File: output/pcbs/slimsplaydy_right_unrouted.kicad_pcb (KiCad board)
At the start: 2 copper layers, 123 x 89.4 mm, 20 parts

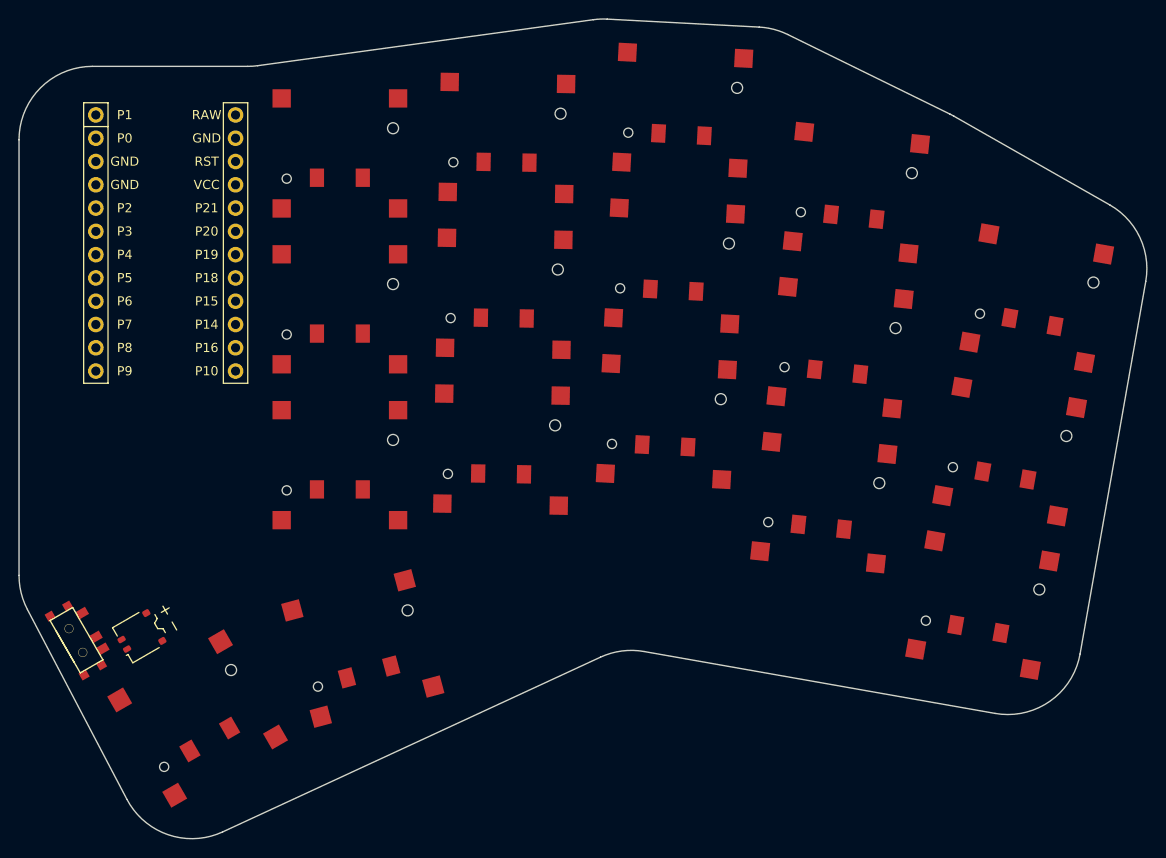
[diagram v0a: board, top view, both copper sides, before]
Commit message: Add battery footprint, change outline.
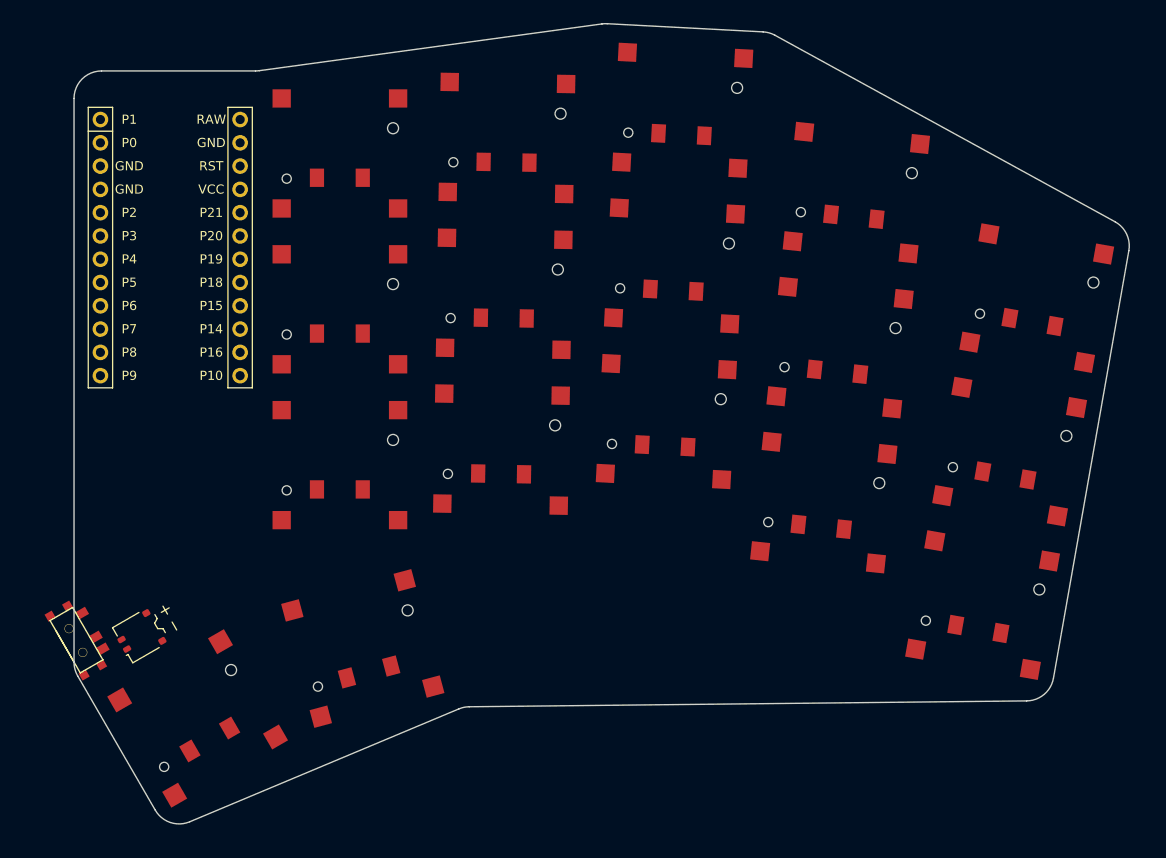
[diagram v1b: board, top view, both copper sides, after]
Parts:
- moved MCU1 0.71 mm to (240.2, 103.4)
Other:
- board size 123 x 89.4 mm -> 115.1 x 87.3 mm
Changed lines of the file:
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@@
   (footprint "ceoloide:mcu_nice_nano"
     (layer "F.Cu")
-    (at 239.71498989999998 102.9119144 0)
+    (at 240.21498989999998 103.4119144 0)
     (property "Reference" "MCU1"
       (at 0 -15 0)
@@
     (fp_line (start 0.45 2.02) (end 0.75 2.52) (layer "F.Fab") (stroke (width 0.1) (type solid)))
   )
-  (gr_line (start 224.62941621776048 144.15640409340858) (end 235.48907572804907 164.87383622286382) (angle 90) (layer Edge.Cuts) (width 0.15))
-(gr_line (start 245.93308625410043 168.4206378744767) (end 287.1447548576141 149.35875036884914) (angle 90) (layer Edge.Cuts) (width 0.15))
-(gr_line (start 291.89237722699136 148.74120448571054) (end 330.1927776020851 155.49459846191698) (angle 90) (layer Edge.Cuts) (width 0.15))
-(gr_line (start 339.4604251055098 149.00532200962266) (end 346.62555657595624 108.36984239288972) (angle 90) (layer Edge.Cuts) (width 0.15))
-(gr_line (start 342.70527937957957 100.02847929984773) (end 325.7106311637271 90.35266764826031) (angle 90) (layer Edge.Cuts) (width 0.15))
-(gr_line (start 325.27590068376344 90.12255661648267) (end 307.56559273611055 81.43431461843029) (angle 90) (layer Edge.Cuts) (width 0.15))
-(gr_line (start 304.46082644944914 80.627566934186) (end 287.8770321181828 79.75844707558387) (angle 90) (layer Edge.Cuts) (width 0.15))
-(gr_line (start 286.3725248782728 79.8215135762144) (end 249.7553757119896 84.83788418286846) (angle 90) (layer Edge.Cuts) (width 0.15))
-(gr_line (start 248.66955648693747 84.9119144) (end 231.71498989999998 84.9119144) (angle 90) (layer Edge.Cuts) (width 0.15))
-(gr_line (start 223.71498989999998 92.9119144) (end 223.71498989999998 140.44228965030038) (angle 90) (layer Edge.Cuts) (width 0.15))
-(gr_arc (start 242.5746494102886 161.15972177975567) (end 235.4890757102886 164.87383617975567) (angle -87.15963248931939) (layer Edge.Cuts) (width 0.15))
-(gr_arc (start 290.5031917014261 156.61966646357) (end 291.8923772014261 148.74120446357) (angle -34.82225270838096) (layer Edge.Cuts) (width 0.15))
-(gr_arc (start 331.58196312765034 147.6161364840575) (end 330.19277762765034 155.49459848405752) (angle -90.00000000000074) (layer Edge.Cuts) (width 0.15))
-(gr_arc (start 338.74709459809674 106.98065686732457) (end 346.62555659809675 108.36984236732457) (angle -70.34521145838565) (layer Edge.Cuts) (width 0.15))
-(gr_arc (start 321.75244638224416 97.30484521573734) (end 325.7106311822442 90.35266761573735) (angle -3.5233551442788595) (layer Edge.Cuts) (width 0.15))
-(gr_arc (start 304.0421384345913 88.61660321768503) (end 307.56559273459135 81.43431461768503) (angle -23.13143158211235) (layer Edge.Cuts) (width 0.15))
-(gr_arc (start 287.45834410332503 87.74748335908288) (end 287.877032103325 79.75844705908288) (angle -10.800686763770258) (layer Edge.Cuts) (width 0.15))
-(gr_arc (start 248.66955648693747 76.9119144) (end 248.66955648693747 84.9119144) (angle -7.80068415589335) (layer Edge.Cuts) (width 0.15))
-(gr_arc (start 231.71498989999998 92.9119144) (end 231.71498989999998 84.9119144) (angle -90) (layer Edge.Cuts) (width 0.15))
-(gr_arc (start 231.71498989999998 140.44228965030038) (end 223.71498989999998 140.44228965030038) (angle -27.662619426405428) (layer Edge.Cuts) (width 0.15))
+  (gr_line (start 230.1175815749614 151.40850733128238) (end 238.5801595902031 166.05106761935943) (angle 90) (layer Edge.Cuts) (width 0.15))
+(gr_line (start 242.33790013594952 167.31643081205561) (end 271.69614917873605 155.00300961504507) (angle 90) (layer Edge.Cuts) (width 0.15))
+(gr_line (start 272.82490909840277 154.76969506548124) (end 333.63407919619016 154.1297000430115) (angle 90) (layer Edge.Cuts) (width 0.15))
+(gr_line (start 336.5569301810632 151.65081072395856) (end 344.78078664705345 105.01100333847262) (angle 90) (layer Edge.Cuts) (width 0.15))
+(gr_line (start 343.26885093801934 101.85961590074882) (end 306.1712679713268 81.51597017246684) (angle 90) (layer Edge.Cuts) (width 0.15))
+(gr_line (start 304.8857883993991 81.1505244358074) (end 287.87730349162115 80.25914752326051) (angle 90) (layer Edge.Cuts) (width 0.15))
+(gr_line (start 287.3147927018884 80.28256782932583) (end 249.91680642992333 85.38438268843433) (angle 90) (layer Edge.Cuts) (width 0.15))
+(gr_line (start 249.51130364514313 85.4119144) (end 232.71498989999998 85.4119144) (angle 90) (layer Edge.Cuts) (width 0.15))
+(gr_line (start 229.71498989999998 88.4119144) (end 229.71498989999998 149.90735117460588) (angle 90) (layer Edge.Cuts) (width 0.15))
+(gr_arc (start 241.17756791524167 164.54991146268293) (end 238.58015951524166 166.05106766268293) (angle -82.72862751199239) (layer Edge.Cuts) (width 0.15))
+(gr_arc (start 272.856481399444 157.76952896441782) (end 272.824909099444 154.76969506441782) (angle -22.151130378445146) (layer Edge.Cuts) (width 0.15))
+(gr_arc (start 333.60250689514885 151.12986614407492) (end 333.63407919514884 154.12970004407492) (angle -79.39700155068272) (layer Edge.Cuts) (width 0.15))
+(gr_arc (start 341.82636336113904 104.49005875858893) (end 344.780786661139 105.01100335858894) (angle -71.26042897747936) (layer Edge.Cuts) (width 0.15))
+(gr_arc (start 304.72878039444646 84.14641303030704) (end 306.17126799444645 81.51597013030704) (angle -25.739569207299766) (layer Edge.Cuts) (width 0.15))
+(gr_arc (start 287.7202954866686 83.25503611776017) (end 287.8773034866686 80.25914751776017) (angle -10.768313705573433) (layer Edge.Cuts) (width 0.15))
+(gr_arc (start 249.51130364514313 82.4119144) (end 249.51130364514313 85.4119144) (angle -7.768311097697847) (layer Edge.Cuts) (width 0.15))
+(gr_arc (start 232.71498989999998 88.4119144) (end 232.71498989999998 85.4119144) (angle -90) (layer Edge.Cuts) (width 0.15))
+(gr_arc (start 232.71498989999998 149.90735117460588) (end 229.71498989999998 149.90735117460588) (angle -30.025500523112385) (layer Edge.Cuts) (width 0.15))
 )

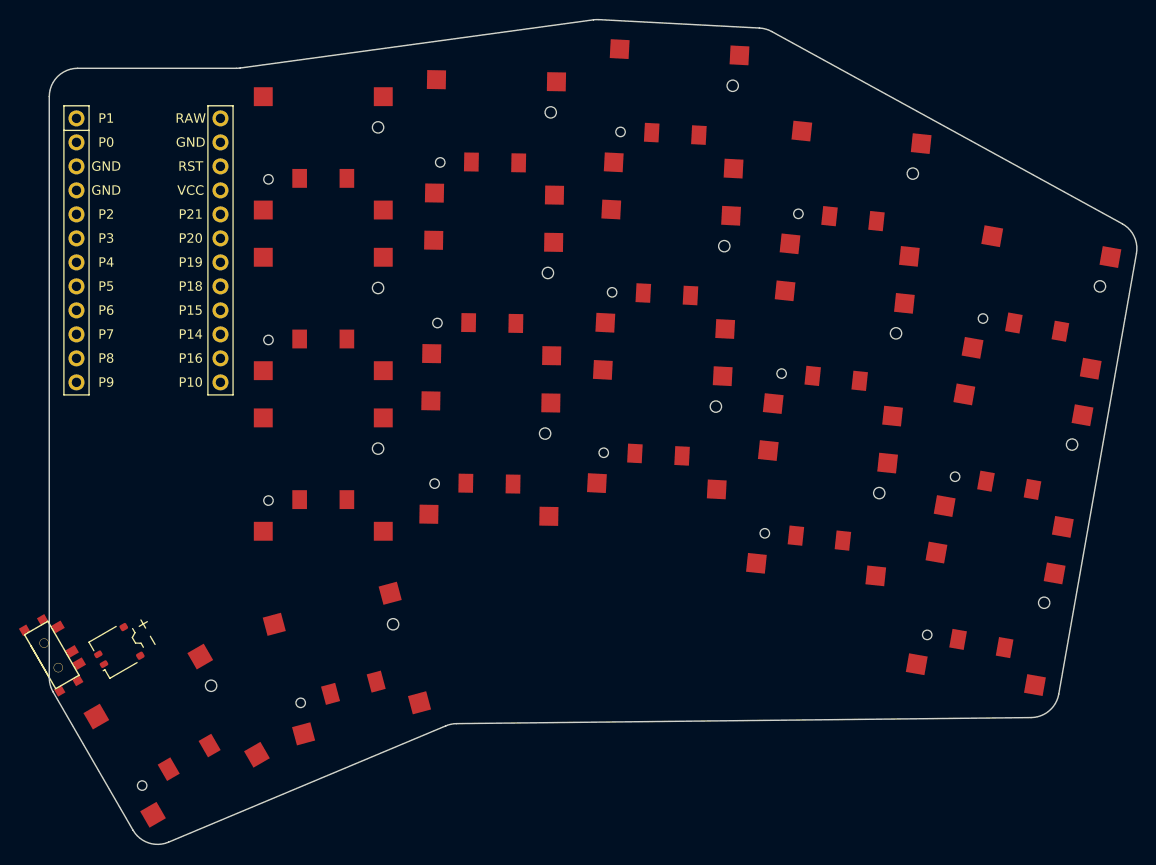
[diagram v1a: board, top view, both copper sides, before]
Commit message: Create first draft design and routing for both sides.
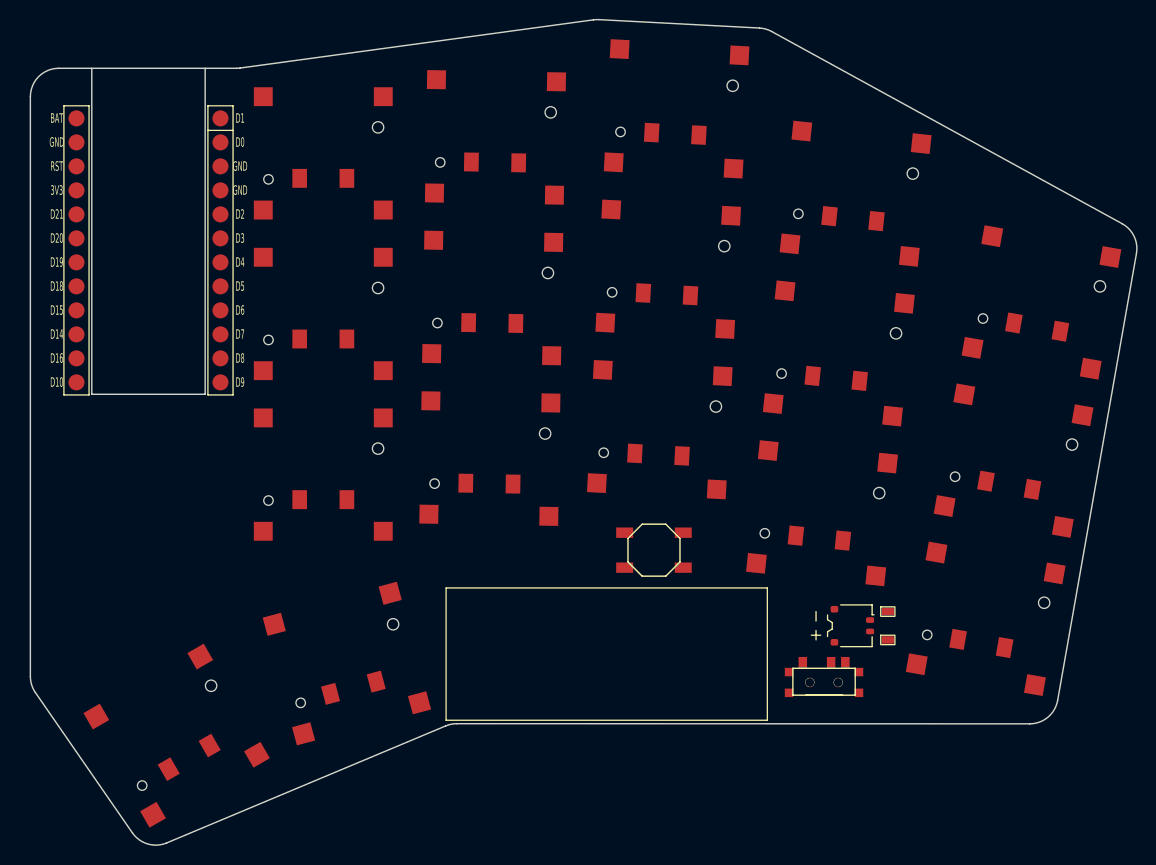
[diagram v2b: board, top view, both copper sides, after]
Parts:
- added B1: , E73:SW_TACT_ALPS_SKQGABE010, F.Cu at (293.7, 136.4)
- added XX1: , Pad_Single, F.Cu at (318.5, 142.9)
- added XX2: , Pad_Single, F.Cu at (318.5, 145.9)
- added XX3: , Battery_301230, F.Cu at (288.7, 147.4)
- moved T1 81.8 mm to (311.7, 150.4), turned to -180 degrees
- moved CONN1 77.9 mm to (314.7, 144.4), turned to -90 degrees
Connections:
- net P2 renamed D21
- MCU1 pad 1: RAW -> mirror_hand_middle_top
- MCU1 pad 10: P14 -> mirror_hand_inner_home
- MCU1 pad 11: P16 -> mirror_hand_ring_home
- MCU1 pad 12: P10 -> mirror_hand_pinky_home
- MCU1 pad 13: P9 -> mirror_hand_pinky_bottom
- MCU1 pad 14: P8 -> mirror_hand_middle_bottom
- MCU1 pad 15: P7 -> mirror_hand_index_bottom
- MCU1 pad 16: P6 -> mirror_hand_inner_bottom
- MCU1 pad 17: P5 -> mirror_hand_ring_bottom
- MCU1 pad 18: P4 -> mirror_thumb_near_fan
- MCU1 pad 19: P3 -> mirror_thumb_far_fan
- MCU1 pad 2: GND -> mirror_hand_index_top
- MCU1 pad 21: GND -> 3V3
- MCU1 pad 22: GND -> RST
- MCU1 pad 23: P0 -> GND
- MCU1 pad 24: P1 -> BAT
- MCU1 pad 3: RST -> GND
- MCU1 pad 4: VCC -> GND
- MCU1 pad 5: P21 -> mirror_hand_inner_top
- MCU1 pad 6: P20 -> mirror_hand_ring_top
- MCU1 pad 7: P19 -> mirror_hand_pinky_top
- MCU1 pad 8: P18 -> mirror_hand_middle_home
- MCU1 pad 9: P15 -> mirror_hand_index_home
- T1 pad 1: BAT -> BAT_P
- T1 pad 2: BAT_P -> BAT
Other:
- board size 115.1 x 87.3 mm -> 117.1 x 87.4 mm

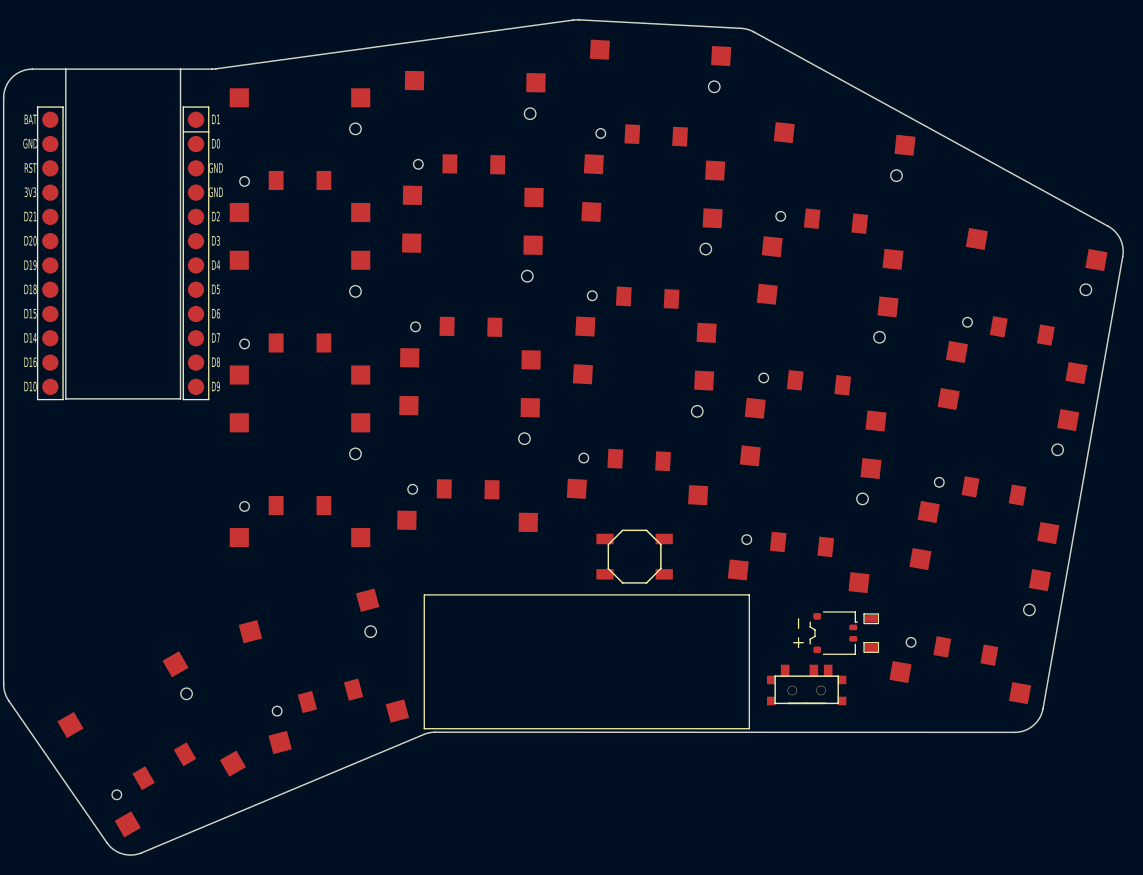
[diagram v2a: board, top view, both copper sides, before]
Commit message: Add new reversable PG1316S footprint.
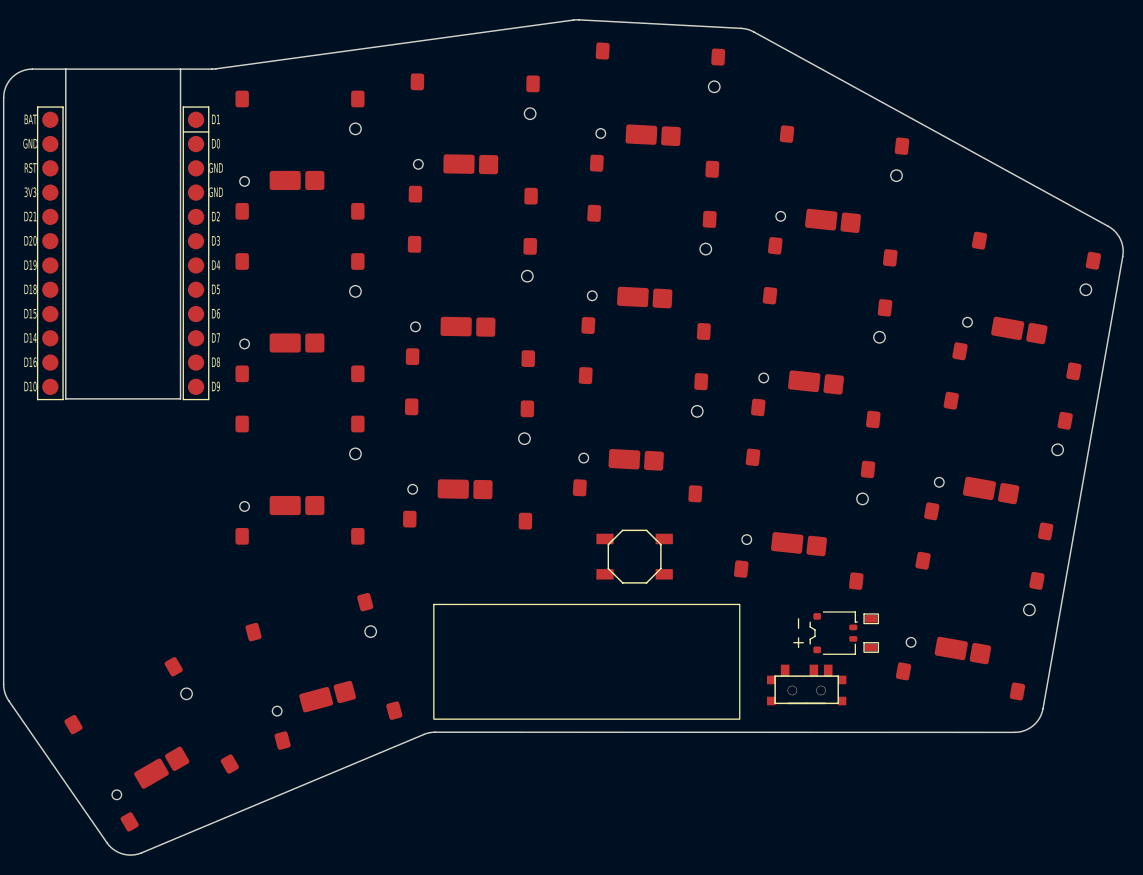
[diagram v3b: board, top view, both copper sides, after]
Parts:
- S1, S10, S11, S12, S13, S14, S15, S16, S17, S2, S3, S4, S5, S6, S7, S8, S9: footprint CPG1316S01D02_mikeholscher -> PG1316S
